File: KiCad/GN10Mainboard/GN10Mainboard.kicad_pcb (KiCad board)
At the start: 4 copper layers, 90 x 68 mm, 127 parts, among them J1 XT30PW-M, J10 USB_C_Receptacle_USB2.0, J12 Conn_01x04, J13 Conn_01x06, J14 Conn_01x06, J4 Conn_01x04, J5 Conn_01x06, J6 Conn_01x04, J7 Conn_01x04, J8 Conn_01x04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

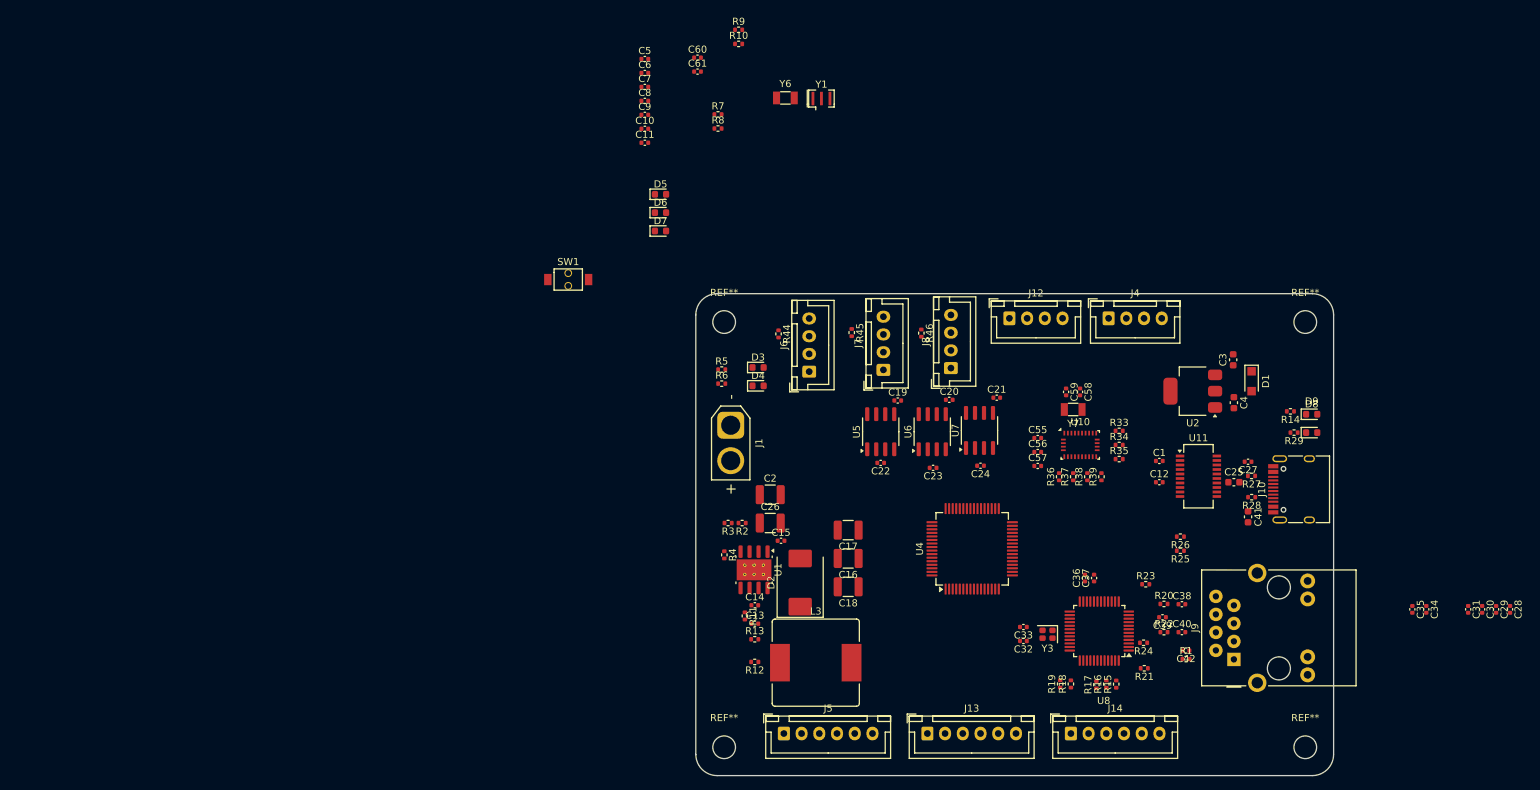
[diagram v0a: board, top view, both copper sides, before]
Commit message: update:parts place
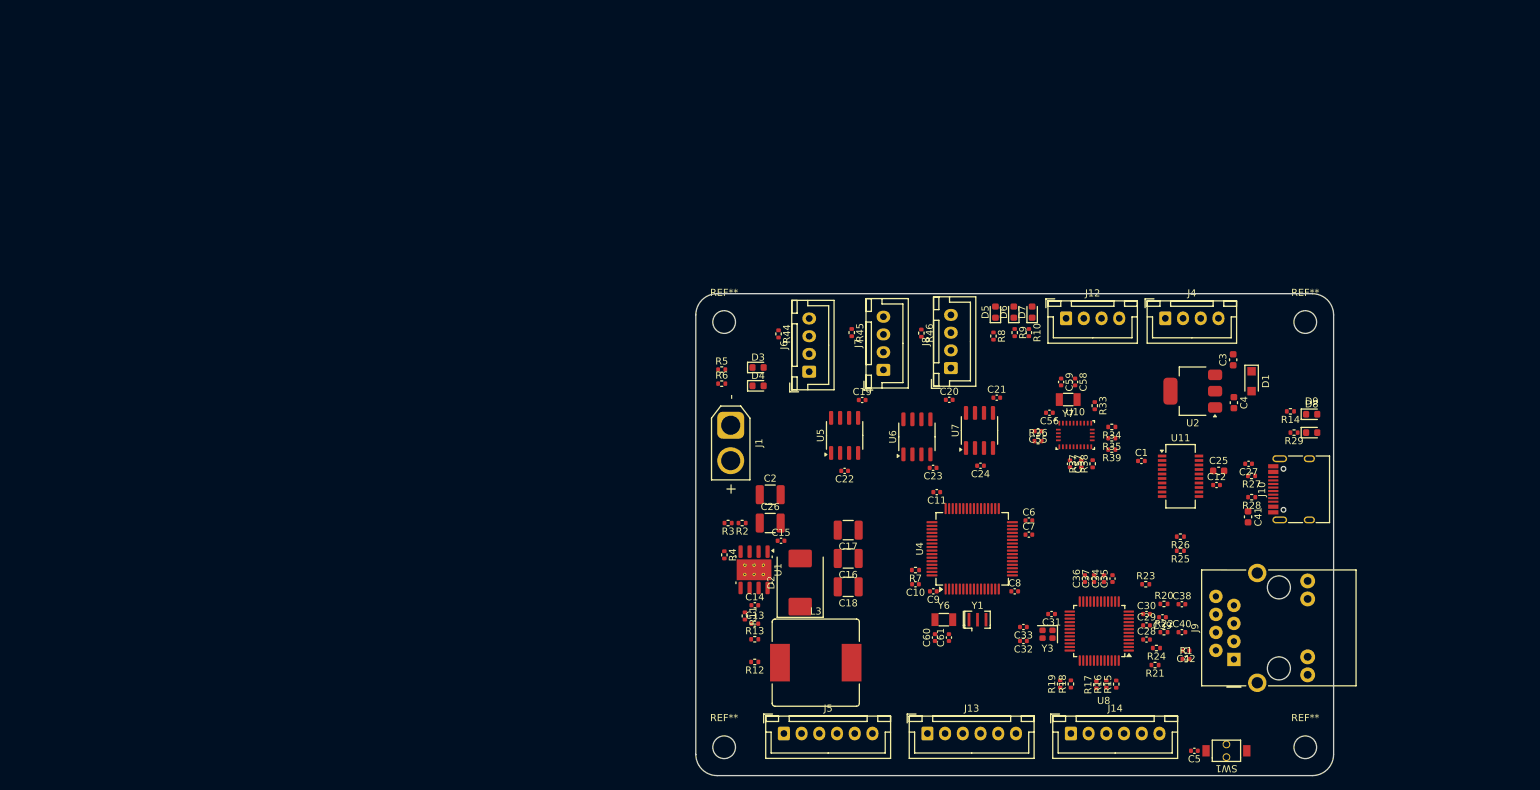
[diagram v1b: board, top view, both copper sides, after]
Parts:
- moved C5 124.7 mm to (200.4, 146.5), turned to 180 degrees
- moved SW1 114.2 mm to (204.9, 146.5), turned to 180 degrees
- moved C60 88.4 mm to (163.8, 130.5), turned to 90 degrees
- moved C61 87.4 mm to (165.7, 130.5), turned to 90 degrees
- moved C8 86.7 mm to (175.0, 124.0)
- moved C7 83.2 mm to (177.0, 116.0)
- moved C6 83.2 mm to (177.0, 114.0)
- moved C9 78.6 mm to (163.5, 124.0), turned to 180 degrees
- moved Y6 76.9 mm to (165.0, 128.0)
- moved Y1 76.8 mm to (169.8, 128.0)
- moved C10 74.8 mm to (161.0, 123.0), turned to 180 degrees
- moved R7 70.1 mm to (161.0, 121.0), turned to 180 degrees
- moved C11 64.2 mm to (164.0, 110.0), turned to 180 degrees
- moved C31 58.8 mm to (180.2, 127.2), turned to 180 degrees
- moved R9 57.8 mm to (175.0, 87.5), turned to -90 degrees
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
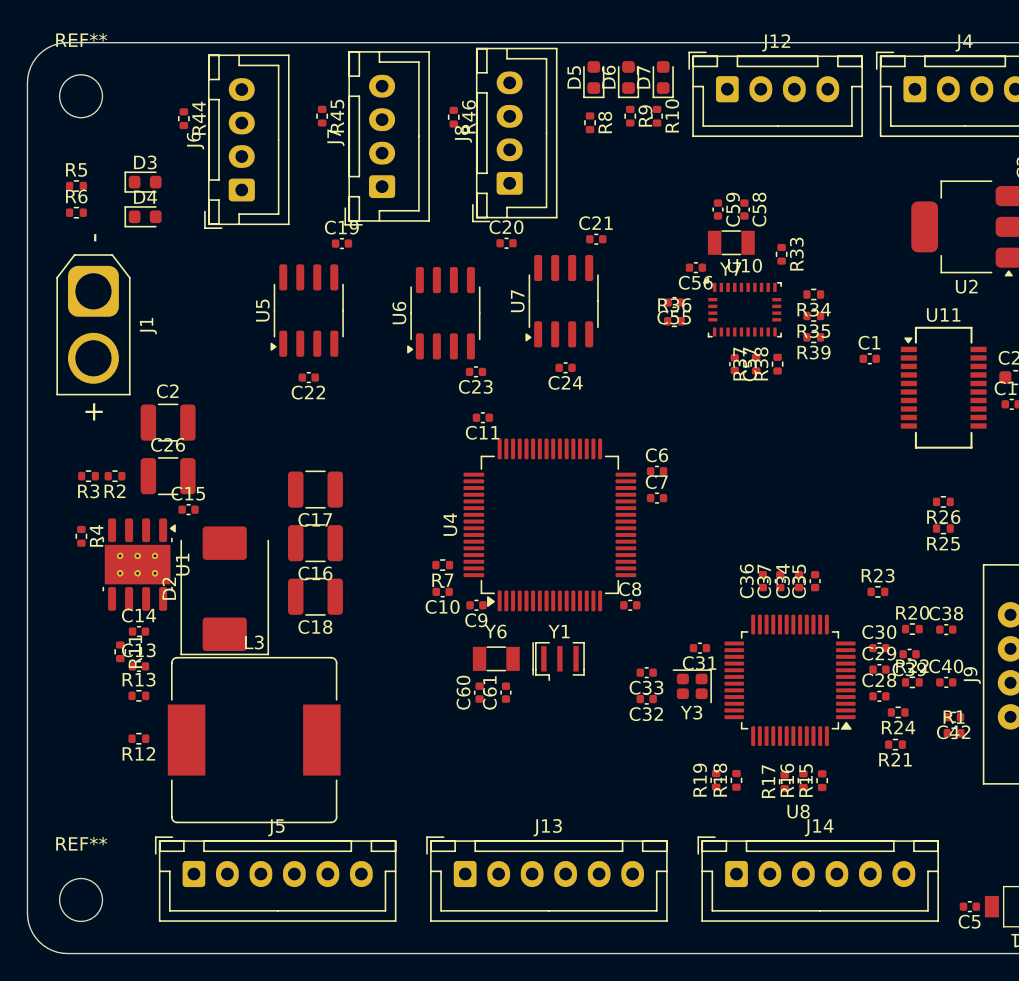
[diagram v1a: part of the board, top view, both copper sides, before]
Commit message: update:footprint
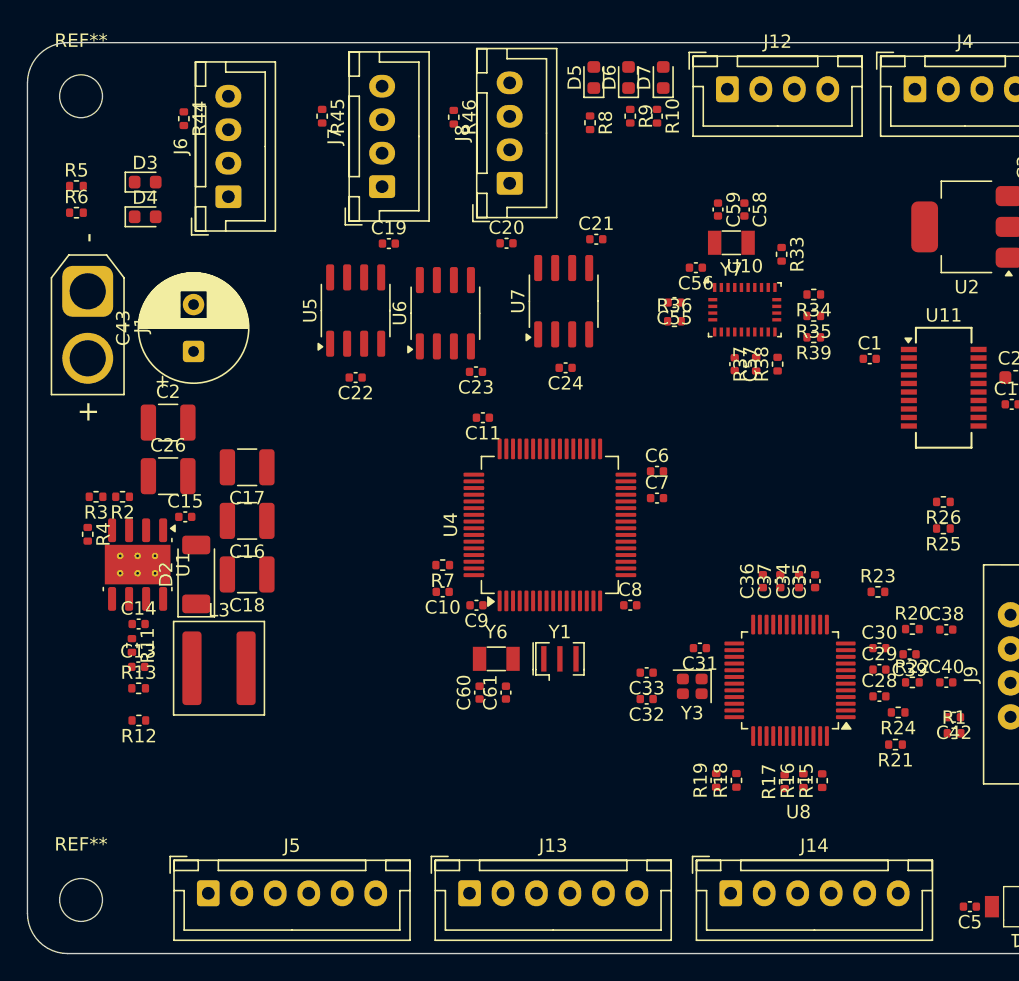
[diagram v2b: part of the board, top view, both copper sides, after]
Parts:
- added C43: 100u, Capacitor_THT:CP_Radial_D8.0mm_P3.50mm, F.Cu at (142.4, 105.1)
- D2: footprint Diode_SMD:D_SMC -> Diode_SMD:D_SOD-128
- L3: footprint Inductor_SMD:L_Bourns_SRR1210A -> Inductor_SMD:L_Coilcraft_XAL6060-XXX
- moved L3 5.97 mm to (144.3, 128.7)
- moved C16 5.37 mm to (146.4, 117.7)
- moved C17 5.37 mm to (146.4, 113.7)
- moved C18 5.37 mm to (146.4, 121.7)
- moved C19 3.50 mm to (157.0, 97.0)
- moved C22 3.50 mm to (154.5, 107.0)
- moved U5 3.50 mm to (154.5, 102.0)
- moved D2 2.38 mm to (142.6, 121.7)
- moved J5 1.79 mm to (143.5, 145.5)
- moved R2 1.64 mm to (137.1, 115.9)
- moved R3 1.64 mm to (135.1, 115.9)
- moved J14 1.50 mm to (182.5, 145.5)
- moved J13 1.47 mm to (163.0, 145.5)
- moved R12 1.36 mm to (138.3, 132.6)
- moved J6 1.12 mm to (145.0, 93.5)
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
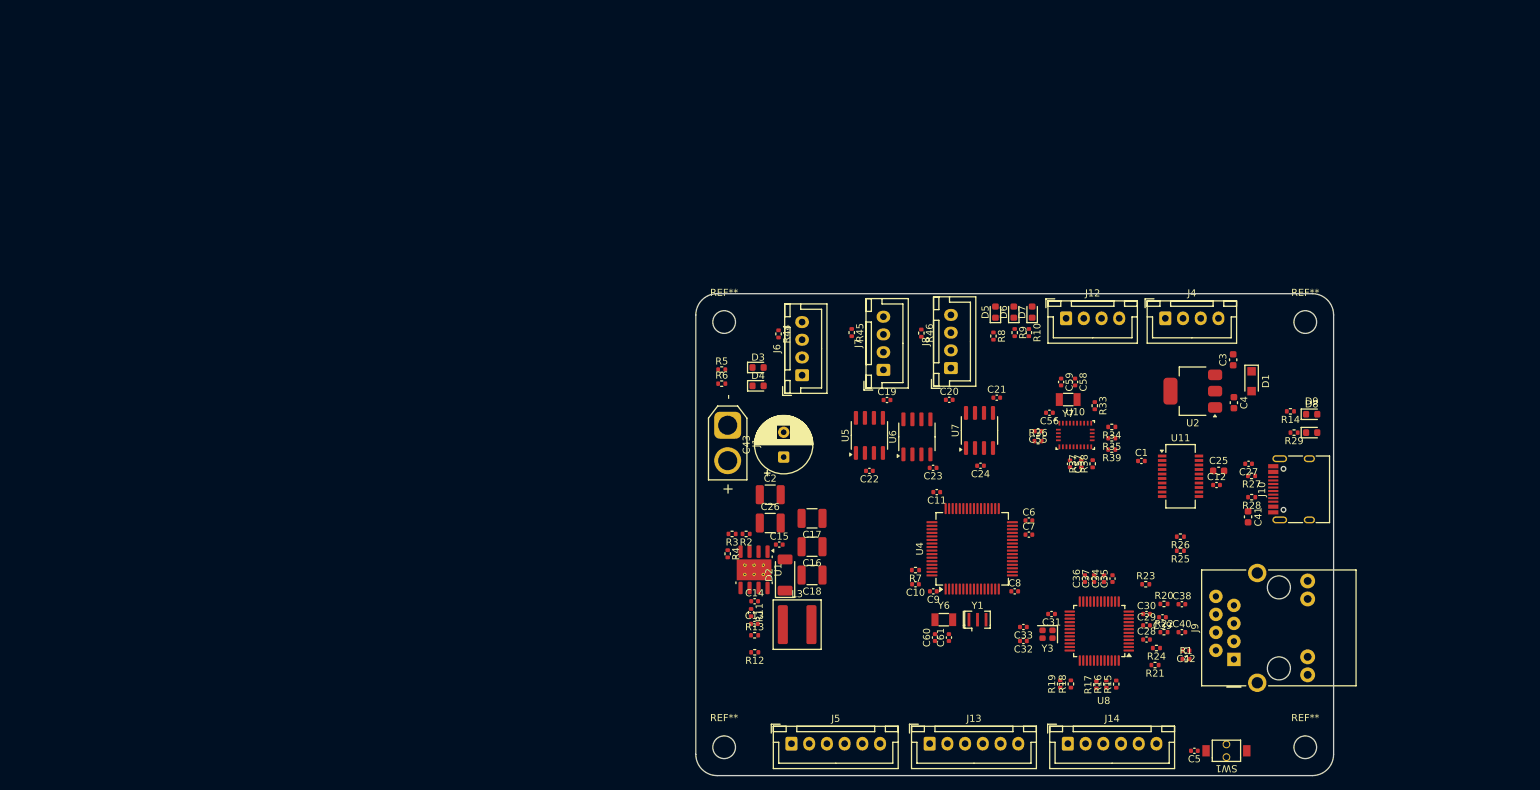
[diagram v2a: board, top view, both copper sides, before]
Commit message: update:board size
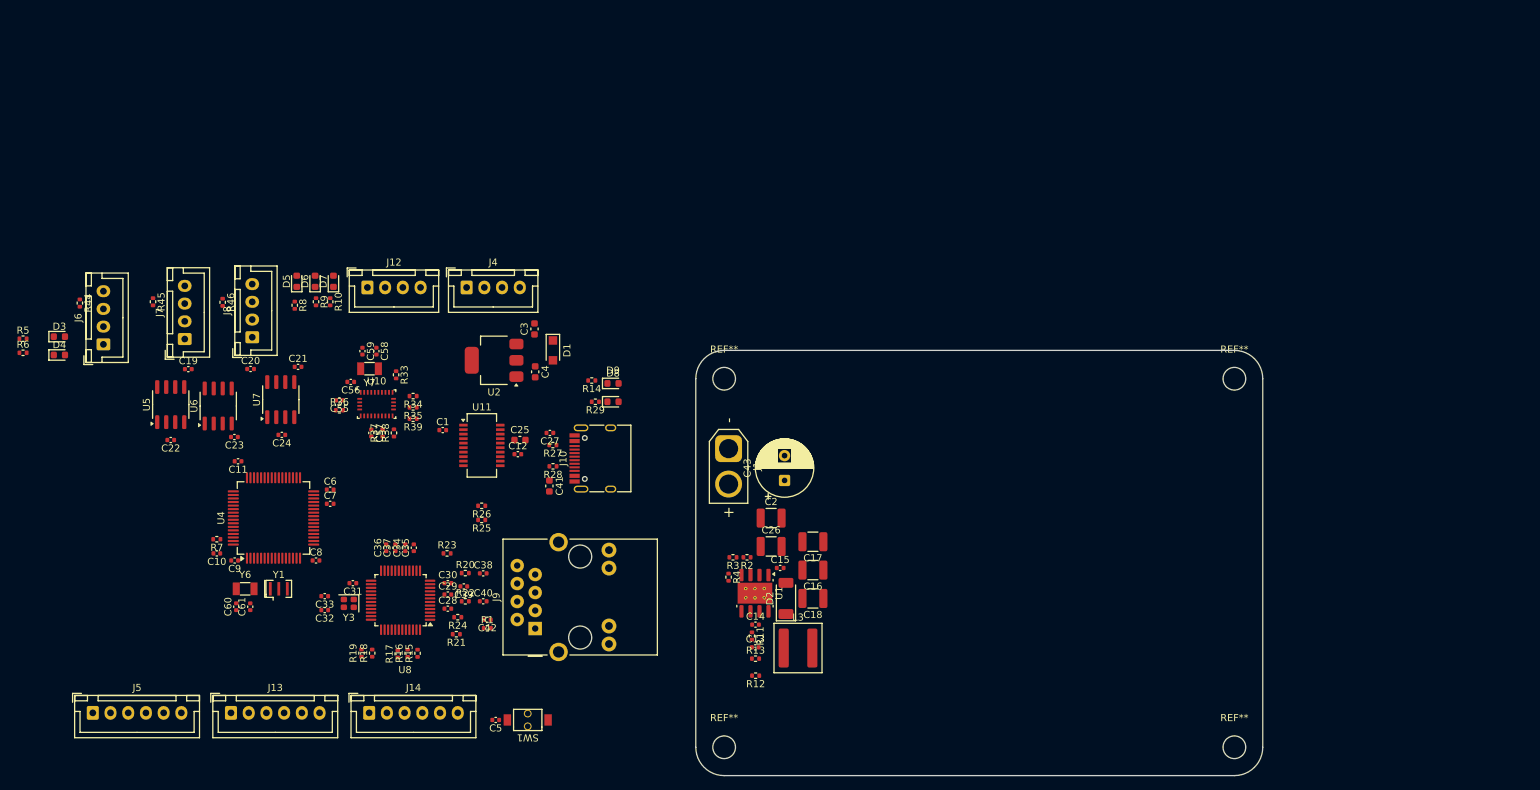
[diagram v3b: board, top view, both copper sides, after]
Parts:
- removed the REF** at (216.0, 146.0)
- removed the REF** at (216.0, 86.0)
- removed the REF** at (134.0, 86.0)
- added REF**: MountingHole_3.2mm_M3, MountingHole:MountingHole_3.2mm_M3, F.Cu at (134.0, 94.0)
- added REF**: MountingHole_3.2mm_M3, MountingHole:MountingHole_3.2mm_M3, F.Cu at (206.0, 146.0)
- added REF**: MountingHole_3.2mm_M3, MountingHole:MountingHole_3.2mm_M3, F.Cu at (206.0, 94.0)
- moved R17 98.7 mm to (87.9, 132.8)
- moved C23 98.7 mm to (64.9, 102.2)
- moved C24 98.7 mm to (71.6, 101.9)
- moved C35 98.7 mm to (90.2, 117.8)
- moved C42 98.7 mm to (100.6, 128.0)
- moved C55 98.7 mm to (79.7, 97.0)
- moved C57 98.7 mm to (84.2, 101.6)
- moved C59 98.7 mm to (83.0, 90.1)
- moved R1 98.7 mm to (100.6, 129.2)
- moved R21 98.7 mm to (96.2, 130.0)
- moved R33 98.7 mm to (87.7, 93.4)
- moved R36 98.7 mm to (79.7, 98.4)
- moved U10 98.7 mm to (85.0, 97.6)
- moved Y7 98.7 mm to (84.0, 92.6)
- moved C10 98.7 mm to (62.4, 118.6)
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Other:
- board size 90 x 68 mm -> 80 x 60 mm

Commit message: update:replace compornent
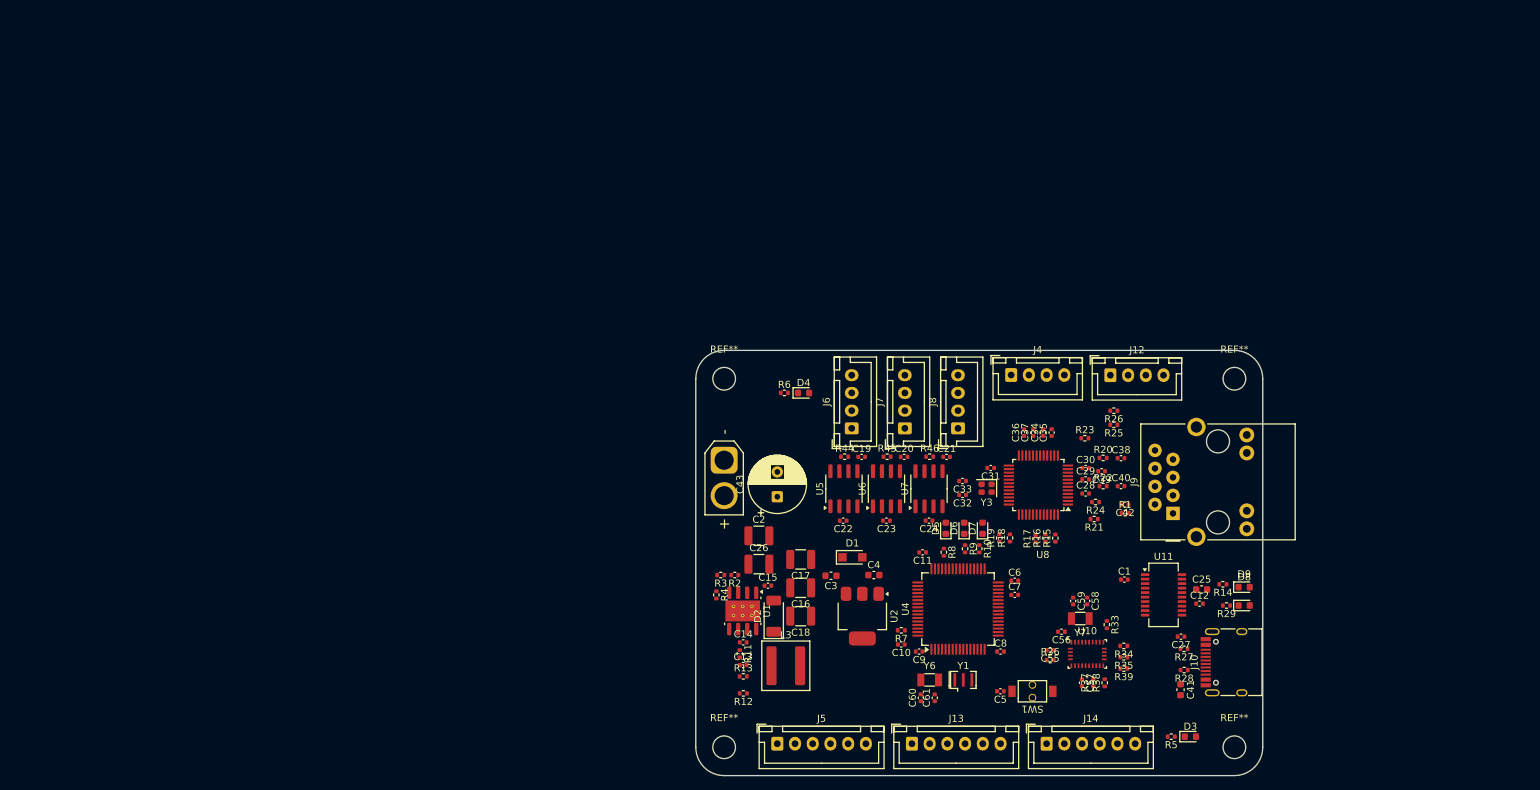
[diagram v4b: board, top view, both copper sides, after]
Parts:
- moved R5 171.5 mm to (197.1, 144.5), turned to 180 degrees
- moved D3 169.3 mm to (199.8, 144.5)
- moved R44 110.1 mm to (151.0, 105.0), turned to 0 degrees
- moved R6 107.6 mm to (142.5, 96.0)
- moved C55 106.3 mm to (180.0, 132.3)
- moved C57 106.3 mm to (184.5, 136.9)
- moved C59 106.3 mm to (183.2, 125.4)
- moved R35 106.3 mm to (190.4, 133.3)
- moved R39 106.3 mm to (190.4, 134.9)
- moved U10 106.3 mm to (185.2, 132.8)
- moved Y7 106.3 mm to (184.2, 127.8)
- moved C58 106.3 mm to (185.2, 125.4)
- moved R37 106.3 mm to (186.1, 136.9)
- moved R38 106.3 mm to (187.7, 136.9)
- moved R33 106.3 mm to (188.0, 128.7)
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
